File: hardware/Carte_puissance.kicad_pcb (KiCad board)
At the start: 2 copper layers, 114 x 57 mm, 41 parts, among them J1 Conn_01x02, J4 MOT LEFT, J5 MOT RIGHT, J6 Conn_01x03, Q1 IPD50P04P4-13, Q2 IPD30N03S4L-09, Q3 IPD30N03S4L-09, SW1 SW_SPDT, U1 MIC4427, U2 MCXA153VLH

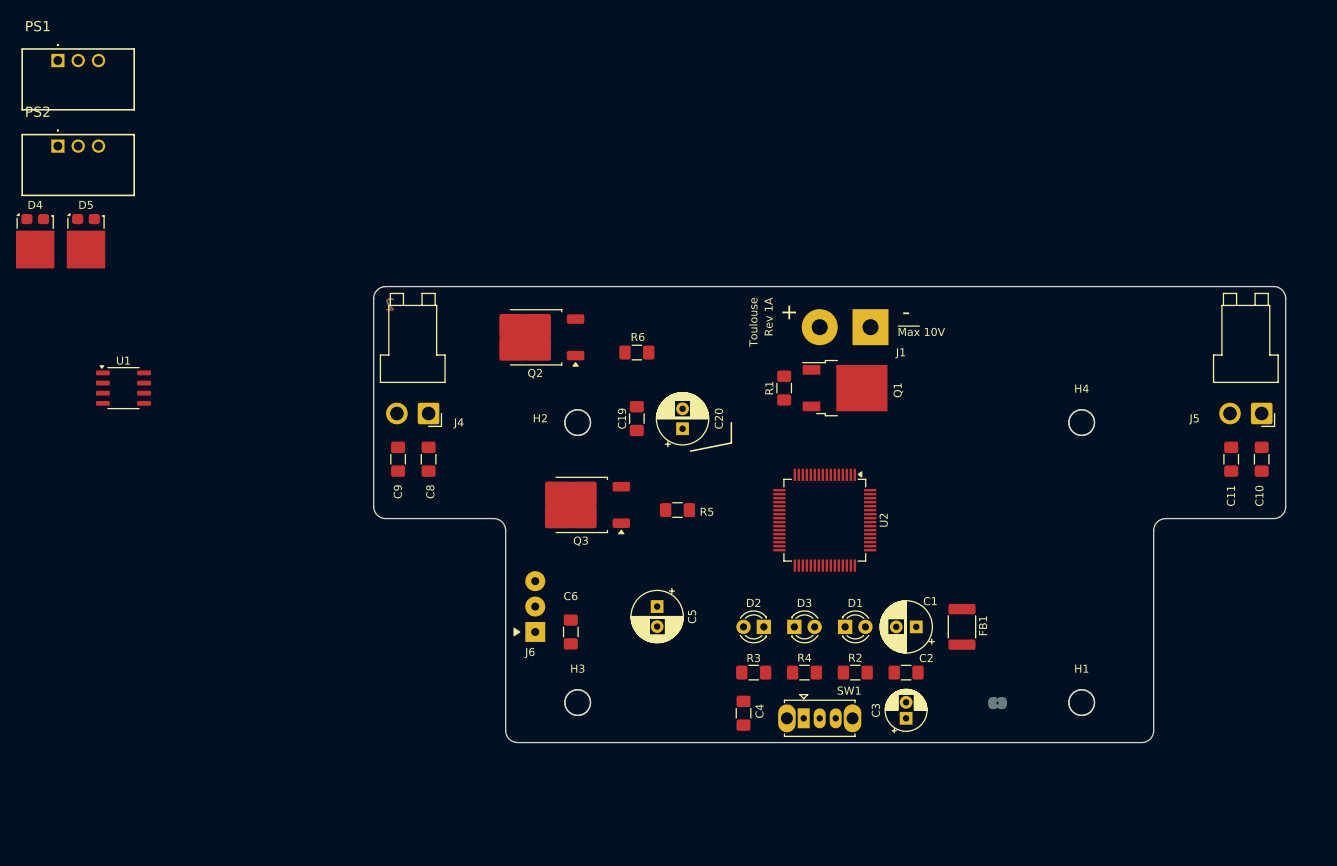
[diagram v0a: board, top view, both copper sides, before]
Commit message: Wip carte alamk pwr 2.0 prete pour tirage
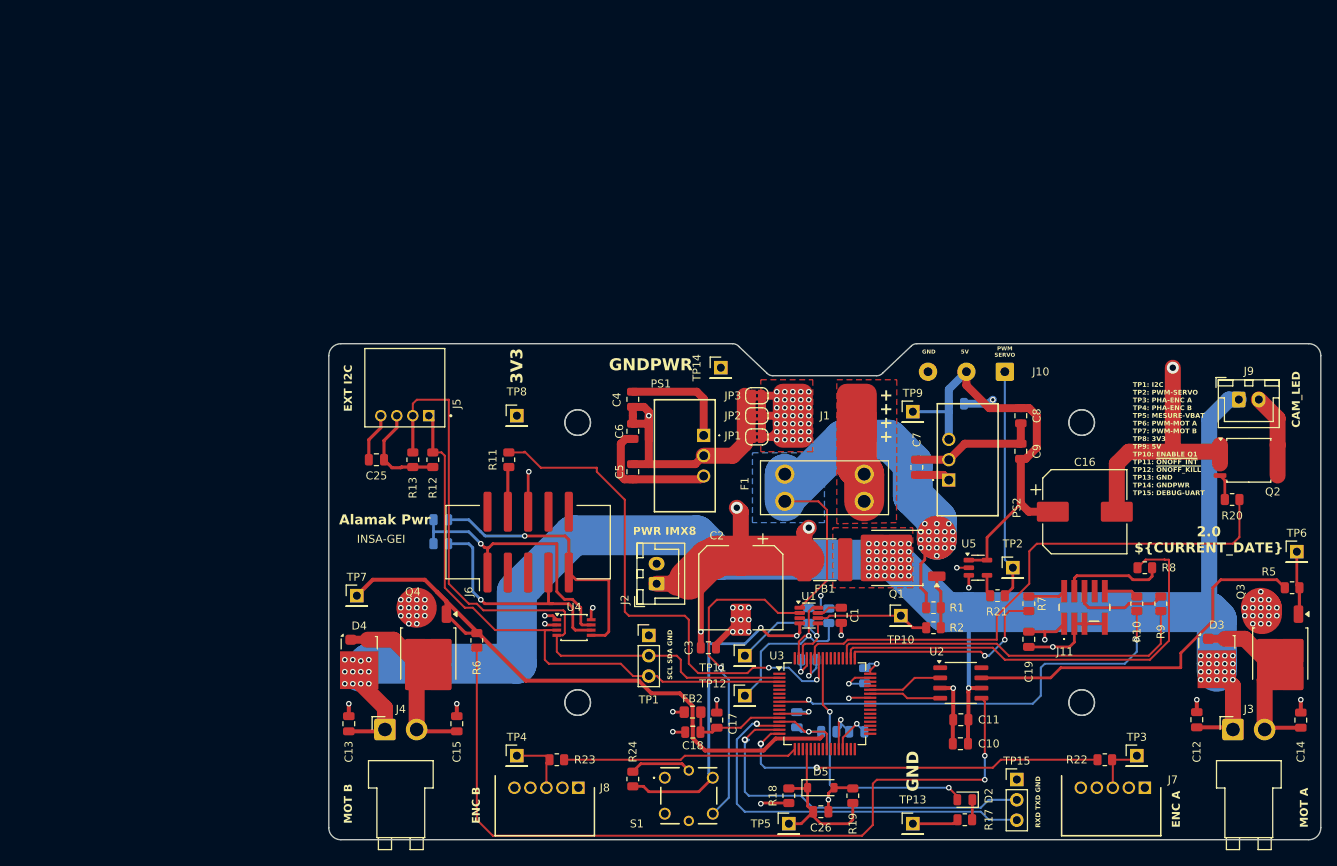
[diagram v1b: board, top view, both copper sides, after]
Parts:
- removed D1: LED, LED_THT:LED_D3.0mm
- removed SW1: SW_SPDT, Button_Switch_THT:SW_Slide_1P2T_CK_OS102011MS2Q
- added C12: 100nF, Capacitor_SMD:C_0805_2012Metric, F.Cu at (202.5, 135.1)
- added C13: 100nF, Capacitor_SMD:C_0805_2012Metric, F.Cu at (96.5, 135.6)
- added C14: 100nF, Capacitor_SMD:C_0805_2012Metric, F.Cu at (215.5, 135.1)
- added C15: 100nF, Capacitor_SMD:C_0805_2012Metric, F.Cu at (110.0, 135.6)
- added C16: 100µF, Capacitor_SMD:CP_Elec_10x10, F.Cu at (188.5, 109.1)
- added C17: 1µF, Capacitor_SMD:C_0805_2012Metric, F.Cu at (142.5, 135.1)
- added C18: 100nF, Capacitor_SMD:C_0805_2012Metric, F.Cu at (139.5, 136.6)
- added C21: 100nF, Capacitor_SMD:C_0805_2012Metric, B.Cu at (161.0, 129.6)
- added C22: 100nF, Capacitor_SMD:C_0805_2012Metric, B.Cu at (156.5, 136.6)
- added C23: 100nF, Capacitor_SMD:C_0805_2012Metric, B.Cu at (152.5, 135.1)
- added C24: 100nF, Capacitor_SMD:C_0805_2012Metric, B.Cu at (160.0, 136.6)
- added C25: 1µF, Capacitor_SMD:C_0805_2012Metric, F.Cu at (99.9, 102.6)
- added C26: 1µF, Capacitor_SMD:C_0805_2012Metric, F.Cu at (155.5, 146.6)
- added C27: 10µF, Capacitor_SMD:C_0805_2012Metric, B.Cu at (172.4, 95.6)
- added C7: 100nF, Capacitor_SMD:C_0805_2012Metric, F.Cu at (167.5, 103.5)
- added F1: Fuse - 5A, 3568:3568, F.Cu at (160.9, 104.4)
- added FB2: MH2029-401Y, Capacitor_SMD:C_0805_2012Metric_Pad1.18x1.45mm_HandSolder, F.Cu at (139.4, 134.1)
- added J10: Cable Servomoteur JST, Connector_Wire:SolderWire-0.5sqmm_1x03_P4.8mm_D0.9mm_OD2.3mm, F.Cu at (178.5, 91.6)
- added J11: FTSH-105-01-L-DV-007-K-TR, FTSH-105-01-L-DV-007:FTSH10501LDV007KTR, F.Cu at (188.4, 121.0)
- added J2: B2B-XH-2, Connector_JST:JST_XH_B2B-XH-A_1x02_P2.50mm_Vertical, F.Cu at (135.0, 118.1)
- added J3: B2PS-VH, Connector_JST:JST_VH_B2PS-VH_1x02_P3.96mm_Horizontal, F.Cu at (207.0, 136.3)
- added J7: DF3A-5P-2DS, DF3A-5P-2DS:SHDRRA5W60P0X200_1X5_1200X720X530P, F.Cu at (196.0, 143.6)
- added J8: DF3A-5P-2DS, DF3A-5P-2DS:SHDRRA5W60P0X200_1X5_1200X720X530P, F.Cu at (125.2, 143.6)
- added J9: B2B-XH-2, Connector_JST:JST_XH_B2B-XH-A_1x02_P2.50mm_Vertical, F.Cu at (207.7, 95.0)
- added JP1: SolderJumper_2_Bridged, Jumper:SolderJumper-2_P1.3mm_Bridged2Bar_RoundedPad1.0x1.5mm, F.Cu at (147.5, 99.7)
- added JP3: SolderJumper_2_Bridged, Jumper:SolderJumper-2_P1.3mm_Bridged2Bar_RoundedPad1.0x1.5mm, F.Cu at (147.5, 94.6)
- added Q4: IPD30N03S4L-09, Package_TO_SOT_SMD:TO-252-2, F.Cu at (106.4, 126.9)
- added R10: 100R, Resistor_SMD:R_0805_2012Metric, F.Cu at (195.0, 120.6)
- added R11: 100R, Resistor_SMD:R_0805_2012Metric, F.Cu at (116.5, 102.6)
- added R12: 4.7K, Resistor_SMD:R_0805_2012Metric, F.Cu at (107.0, 102.6)
- added R13: 4.7K, Resistor_SMD:R_0805_2012Metric, F.Cu at (104.5, 102.6)
- added R14: 4.7K, Resistor_SMD:R_0805_2012Metric, B.Cu at (108.0, 113.1)
- added R15: 4.7K, Resistor_SMD:R_0805_2012Metric, B.Cu at (108.0, 110.1)
- added R17: 750R, Resistor_SMD:R_0805_2012Metric, F.Cu at (173.5, 147.6)
- added R18: 18K, Resistor_SMD:R_0805_2012Metric, F.Cu at (151.5, 144.6)
- added R19: 10K, Resistor_SMD:R_0805_2012Metric, F.Cu at (159.5, 144.6)
- added R20: 10R, Resistor_SMD:R_0805_2012Metric, F.Cu at (206.9, 107.5)
- added R21: 100R, Resistor_SMD:R_0805_2012Metric, F.Cu at (177.6, 119.6)
- added R22: 100R, Resistor_SMD:R_0805_2012Metric, F.Cu at (191.0, 140.1)
- added R23: 100R, Resistor_SMD:R_0805_2012Metric, F.Cu at (122.5, 140.1)
- added R24: 330R, Resistor_SMD:R_0805_2012Metric, F.Cu at (132.0, 142.5)
- added R7: 100R, Resistor_SMD:R_0805_2012Metric, F.Cu at (181.5, 120.6)
- added R8: 100R, Resistor_SMD:R_0805_2012Metric, F.Cu at (196.0, 116.1)
- added R9: 100R, Resistor_SMD:R_0805_2012Metric, F.Cu at (198.0, 120.6)
- added S1: TL1265BQSCLR, TL1265BQSCLR:TL1265BQSCLR, F.Cu at (136.0, 142.3)
- added TP1: Conn_01x03_Pin, Connector_PinHeader_2.54mm:PinHeader_1x03_P2.54mm_Vertical, F.Cu at (134.0, 124.5)
- added TP10: TestPoint, Connector_PinHeader_2.54mm:PinHeader_1x01_P2.54mm_Vertical, F.Cu at (165.5, 122.1)
- added TP11: TestPoint, Connector_PinHeader_2.54mm:PinHeader_1x01_P2.54mm_Vertical, F.Cu at (146.0, 127.1)
- added TP12: TestPoint, Connector_PinHeader_2.54mm:PinHeader_1x01_P2.54mm_Vertical, F.Cu at (146.0, 132.1)
- added TP13: TestPoint, Connector_PinHeader_2.54mm:PinHeader_1x01_P2.54mm_Vertical, F.Cu at (167.0, 148.1)
- added TP14: TestPoint, Connector_PinHeader_2.54mm:PinHeader_1x01_P2.54mm_Vertical, F.Cu at (143.0, 91.1)
- added TP15: Conn_01x03_Pin, Connector_PinHeader_2.54mm:PinHeader_1x03_P2.54mm_Vertical, F.Cu at (180.0, 142.5)
- added TP2: TestPoint, Connector_PinHeader_2.54mm:PinHeader_1x01_P2.54mm_Vertical, F.Cu at (179.5, 116.1)
- added TP3: TestPoint, Connector_PinHeader_2.54mm:PinHeader_1x01_P2.54mm_Vertical, F.Cu at (195.0, 139.6)
- added TP4: TestPoint, Connector_PinHeader_2.54mm:PinHeader_1x01_P2.54mm_Vertical, F.Cu at (117.5, 139.6)
- added TP5: TestPoint, Connector_PinHeader_2.54mm:PinHeader_1x01_P2.54mm_Vertical, F.Cu at (151.5, 148.1)
- added TP6: TestPoint, Connector_PinHeader_2.54mm:PinHeader_1x01_P2.54mm_Vertical, F.Cu at (215.0, 114.1)
- added TP7: TestPoint, Connector_PinHeader_2.54mm:PinHeader_1x01_P2.54mm_Vertical, F.Cu at (97.5, 119.6)
- added TP8: TestPoint, Connector_PinHeader_2.54mm:PinHeader_1x01_P2.54mm_Vertical, F.Cu at (117.5, 97.1)
- added TP9: TestPoint, Connector_PinHeader_2.54mm:PinHeader_1x01_P2.54mm_Vertical, F.Cu at (167.0, 96.6)
- added U3: MCXA153VLH, Package_QFP:LQFP-64_10x10mm_P0.5mm, F.Cu at (156.0, 133.1)
- added U4: PCA9306DP, Package_SO:TSSOP-8_3x3mm_P0.65mm, F.Cu at (124.6, 123.5)
- added U5: 74AHC1G126, Package_TO_SOT_SMD:SOT-23-5, F.Cu at (175.1, 116.1)
- C1: value 100µF -> 1µF; footprint Capacitor_THT:CP_Radial_D6.3mm_P2.50mm -> Capacitor_SMD:C_0805_2012Metric
- C10, C4, C8: footprint Capacitor_SMD:C_1206_3216Metric_Pad1.42x1.75mm_HandSolder -> Capacitor_SMD:C_0805_2012Metric
- C11, C6, C9: value 100nF -> 10µF; footprint Capacitor_SMD:C_1206_3216Metric_Pad1.42x1.75mm_HandSolder -> Capacitor_SMD:C_0805_2012Metric
- C19: value 100nF -> 470nF; footprint Capacitor_SMD:C_1206_3216Metric_Pad1.42x1.75mm_HandSolder -> Capacitor_SMD:C_0805_2012Metric
- C2: value 100nF -> 100µF; footprint Capacitor_SMD:C_1206_3216Metric_Pad1.42x1.75mm_HandSolder -> Capacitor_SMD:CP_Elec_10x10
- C20: value 470µF -> 100nF; footprint Capacitor_THT:CP_Radial_D6.3mm_P2.50mm -> Capacitor_SMD:C_0805_2012Metric; moved to B.Cu
- C3: footprint Capacitor_THT:CP_Radial_D5.0mm_P2.00mm -> Capacitor_SMD:C_0805_2012Metric
- C5: value 100µF -> 100nF; footprint Capacitor_THT:CP_Radial_D6.3mm_P2.50mm -> Capacitor_SMD:C_0805_2012Metric
- D2: value LED -> LED Rouge; footprint LED_THT:LED_D3.0mm -> LED_SMD:LED_0805_2012Metric
- D3: value LED -> STPS1230SF; footprint LED_THT:LED_D3.0mm -> Package_TO_SOT_SMD:TO-277A
- D5: value STPS1230SF -> MMSZ3V3T1G; footprint Package_TO_SOT_SMD:TO-277A -> Diode_SMD:D_SOD-123
- FB1: value Ferrite_Bead -> 7427928801; footprint Capacitor_SMD:C_1812_4532Metric_Pad1.30x3.40mm_HandSolder -> Capacitor_SMD:C_2220_5750Metric
- J1: value Conn_01x02 -> Cable XT60; footprint Connector_Wire:SolderWirePad_1x02_P7.62mm_Drill2mm -> Battery_Pads:Battery_Pads
- J4: value MOT LEFT -> B2PS-VH
- J5: value MOT RIGHT -> SeedStudio 110990037; footprint Connector_JST:JST_VH_B2PS-VH_1x02_P3.96mm_Horizontal -> Seeed Studio 110990037:SEEED_110990037
- J6: value Conn_01x03 -> 72454-010VLF; footprint Connector_Wire:SolderWirePad_1x03_P3.175mm_Drill1mm -> Connector_IDC:IDC-Header_2x05_P2.54mm_Vertical_SMD
- JP2: moved to F.Cu
- Q1: value IPD50P04P4-13 -> IPD50P04P413ATMA2
- Q2: value IPD30N03S4L-09 -> TPH2R506PL,L1Q; footprint Package_TO_SOT_SMD:TO-252-2 -> Package_SO:SOP-8_5.28x5.23mm_P1.27mm
- R1: value 10K -> 100K; footprint Resistor_SMD:R_1206_3216Metric_Pad1.42x1.75mm_HandSolder -> Resistor_SMD:R_0805_2012Metric
- R2: value 470R -> 100K; footprint Resistor_SMD:R_1206_3216Metric_Pad1.42x1.75mm_HandSolder -> Resistor_SMD:R_0805_2012Metric
- R3: value 220R -> 10K; footprint Resistor_SMD:R_1206_3216Metric_Pad1.42x1.75mm_HandSolder -> Resistor_SMD:R_0805_2012Metric; moved to B.Cu
- R4: value 100R -> 10K; footprint Resistor_SMD:R_1206_3216Metric_Pad1.42x1.75mm_HandSolder -> Resistor_SMD:R_0805_2012Metric; moved to B.Cu
- R5, R6: value 10K -> 10R; footprint Resistor_SMD:R_1206_3216Metric_Pad1.42x1.75mm_HandSolder -> Resistor_SMD:R_0805_2012Metric
- U1: value MIC4427 -> LTC2954CTS8-2#TRMPBF; footprint Package_SO:SO-8_3.9x4.9mm_P1.27mm -> Package_TO_SOT_SMD:SOT-23-8
- U2: value MCXA153VLH -> MIC4427; footprint Package_QFP:LQFP-64_10x10mm_P0.5mm -> Package_SO:SO-8_3.9x4.9mm_P1.27mm
- moved PS2 118.9 mm to (171.5, 105.1), turned to 90 degrees
- moved D5 114.5 mm to (155.5, 143.6)
- moved J5 107.2 mm to (103.5, 93.6)
- moved PS1 93.3 mm to (140.8, 99.5), turned to -90 degrees
- moved Q2 90.5 mm to (209.0, 102.6), turned to 0 degrees
- moved U1 90.3 mm to (154.0, 122.0)
- moved Q3 89.4 mm to (212.9, 126.9), turned to -90 degrees
- moved C9 77.8 mm to (180.5, 101.5), turned to 90 degrees
- moved R5 77.4 mm to (214.4, 118.6)
- moved C8 74.2 mm to (180.5, 97.1), turned to -90 degrees
- moved D4 66.4 mm to (97.8, 127.8)
- moved C19 56.2 mm to (181.5, 125.0), turned to -90 degrees
- moved D3 53.0 mm to (205.0, 127.7)
- moved C10 51.8 mm to (172.9, 138.1), turned to 180 degrees
- moved C11 46.9 mm to (173.0, 135.1), turned to 180 degrees
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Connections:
- C1 pad 1: VCC -> Net-(U1-PDT)
- C1 pad 2: GND -> GNDPWR
- C10 pad 1: GNDPWR -> +BATT
- C10 pad 2: +BATT -> GNDPWR
- C11 pad 1: Net-(D5-A) -> +BATT
- C19 pad 1: +BATT -> +3.3V
- C19 pad 2: GNDPWR -> GND
- C20 pad 1: +BATT -> +3.3V
- C20 pad 2: GNDPWR -> GND
- C3 pad 1: +3V3 -> VCC
- C5 pad 1: +5V -> +3.3V
- C5 pad 2: GNDA -> GND
- C6 pad 1: GNDA -> +3.3V
- C6 pad 2: +5V -> GND
- C8 pad 1: GNDPWR -> +5V
- C8 pad 2: +BATT -> GNDPWR
- C9 pad 1: Net-(D4-A) -> +5V
- D2 pad 2: +5V -> /CPU/ALERT_LED
- D3 pad 1: Net-(D3-K) -> Net-(J3-Pin_2)
- D3 pad 2: +3.3V -> Net-(J3-Pin_2)
- D4 pad 1: +BATT -> Net-(J4-Pin_2)
- D4 pad 2: Net-(D4-A) -> Net-(J4-Pin_2)
- D4 pad 3: (no net) -> +BATT
- D5 pad 1: +BATT -> /CPU/MESURE_ADC
- D5 pad 2: Net-(D5-A) -> GND
- FB1 pad 1: VCC -> +BATT
- FB1 pad 2: +BATT -> VCC
- J4 pad 2: Net-(D4-A) -> Net-(J4-Pin_2)
- J5 pad 1: +BATT -> /CPU/I2C_SCL
- J5 pad 2: Net-(D5-A) -> /CPU/I2C_SDA
- J6 pad 1: /SERVO_PWM -> /IO/3V3_IMX8MP
- J6 pad 2: +5V -> unconnected-(J6-Pin_2-Pad2)
- J6 pad 3: GNDA -> unconnected-(J6-Pin_3-Pad3)
- PS2 pad 2: GND -> GNDPWR
- Q1 pad 3: Net-(J1-Pin_2) -> Net-(Q1-S)
- Q2 pad 1: Net-(Q2-G) -> GNDPWR
- Q2 pad 2: Net-(D4-A) -> GNDPWR
- Q3 pad 2: Net-(D5-A) -> Net-(J3-Pin_2)
- R1 pad 1: Net-(J1-Pin_2) -> Net-(Q1-S)
- R2 pad 1: Net-(D1-K) -> Net-(U1-EN/~{EN})
- R2 pad 2: GND -> Net-(Q1-G)
- R3 pad 1: Net-(D2-K) -> +3.3V
- R3 pad 2: GND -> /CPU/~{ONOFF_INT}
- R4 pad 1: Net-(D3-K) -> +3.3V
- R4 pad 2: GND -> /CPU/~{ONOFF_KILL}
- R5 pad 1: /DISABLE_MOT_L -> Net-(Q3-G)
- R5 pad 2: Net-(Q3-Pad3) -> Net-(U2-OUT_A)
- R6 pad 1: /DISABLE_MOT_L -> Net-(U2-OUT_B)
- U1 pad 1: unconnected-(U1-NC-Pad1) -> Net-(Q1-S)
- U1 pad 2: unconnected-(U1-IN_A-Pad2) -> Net-(S1-NO_4)
- U1 pad 3: GNDPWR -> unconnected-(U1-ONT-Pad3)
- U1 pad 4: unconnected-(U1-IN_B-Pad4) -> GNDPWR
- U1 pad 5: Net-(U1-OUT_B) -> /CPU/~{ONOFF_INT}
- U1 pad 6: +BATT -> Net-(U1-EN/~{EN})
- U1 pad 7: Net-(U1-OUT_A) -> Net-(U1-PDT)
- U1 pad 8: unconnected-(U1-NC-Pad8) -> /CPU/~{ONOFF_KILL}
- U2 pad 2: unconnected-(U2-P1_8/WUU0_IN10/LPUART1_RXD/LPI2C0_SDA/CT_INP8/CT0_MAT2/I3C0_SDA-Pad2) -> /CPU/MOTOR_A_PWM
- U2 pad 3: unconnected-(U2-P1_9/LPUART1_TXD/LPI2C0_SCL/CT_INP9/CT0_MAT3/I3C0_SCL-Pad3) -> GNDPWR
- U2 pad 4: unconnected-(U2-P1_10/LPUART1_RTS_B/LPI2C0_SDAS/CT2_MAT0/ADC0_A8-Pad4) -> /CPU/MOTOR_B_PWM
- U2 pad 5: unconnected-(U2-P1_11/WUU0_IN11/TRIG_OUT2/LPUART1_CTS_B/LPI2C0_SCLS/CT2_MAT1/I3C0_PUR/ADC0_A9-Pad5) -> Net-(U2-OUT_B)
- U2 pad 6: unconnected-(U2-P1_12/WUU0_IN12/LPUART2_RXD/CT2_MAT2/ADC0_A10-Pad6) -> +BATT
- U2 pad 7: unconnected-(U2-P1_13/TRIG_IN3/LPUART2_TXD/CT2_MAT3/ADC0_A11-Pad7) -> Net-(U2-OUT_A)
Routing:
- net GNDPWR: track 0.00 -> 408.8 mm, vias 0 -> 76
- net +BATT: track 0.00 -> 202.5 mm, vias 0 -> 63
- net VCC: track 0.00 -> 122.1 mm, vias 0 -> 4
- net GND: track 0.00 -> 108.7 mm, vias 0 -> 21
- net Net-(U2-OUT_B): track 0.00 -> 102.1 mm, vias 0 -> 2
- net /CPU/I2C_SDA: track 0.00 -> 85.6 mm
- net Net-(Q4-G): track 0.00 -> 79.0 mm
- net /CPU/I2C_SCL: track 0.00 -> 74.0 mm
- net /CPU/CMD_CAMERA_LED: track 0.00 -> 69.0 mm
- net +3.3V: track 0.00 -> 68.7 mm, vias 0 -> 9
- net /CPU/ONOFF_IMX8MP: track 0.00 -> 65.5 mm, vias 0 -> 2
- net Net-(Q1-S): track 0.00 -> 65.5 mm, vias 0 -> 19
- net /CPU/SWCLK: track 0.00 -> 57.0 mm
- net /CPU/nRESET: track 0.00 -> 54.8 mm, vias 0 -> 2
- net +5V: track 0.00 -> 53.6 mm
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- added copper zone on In1.Cu, net +3.3V
- added copper zone on F.Cu, net +BATT
- added copper zone on In2.Cu, net GND
- added copper zone on F.Cu, net GNDPWR
- added copper zone on In2.Cu, net GNDPWR
- added copper zone on F.Cu, net Net-(J1-Pin_2)
- added copper zone on B.Cu, net Net-(Q1-S)
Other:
- board size 114 x 57 mm -> 124 x 62 mm
- copper layers 2 -> 4
- rule pad_to_mask_clearance: 0.051 -> 0
- board text added: "${COMPANY}"
- board text added: "${REVISION} ${CURRENT_DATE}"
- board text added: "${TITLE}"
- board text added: "++++"
- board text added: "3V3"
- board text added: "5V"
- board text added: "Arriere"
- board text added: "Avant"
- board text added: "CAM_LED"
- board text added: "ENC A"
- board text added: "ENC B"
- board text added: "EXT I2C"
- board text added: "GND"
- board text added: "GNDPWR"
- board text added: "IDX 3.3V PHA PHB GND"
- board text added: "MOT A"
- board text added: "MOT B"
- board text added: "PWM SERVO"
- board text added: "PWR IMX8"
- board text added: "RXD TXD GND"
- board text added: "SCL SDA 3.3V GND"
- board text added: "SCL SDA GND"
- board text added: "TP1: I2C TP2: PWM-SERVO TP3: PHA-ENC A TP4: PHA-ENC B TP5: MESURE-VBAT TP6: PWM-MOT A TP7: PWM-MOT B TP8: 3V3 TP9: 5V TP10: ENABLE Q1 TP11: ~{ONOFF_INT} TP12: ~{ONOFF_KILL} TP13: GND TP14: GNDPWR TP15: DEBUG-UART"
- board text removed: "+"
- board text removed: "-"
- board text removed: "1"
- board text removed: "2"
- board text removed: "Rev 1A"
- board text removed: "Toulouse"
- board text removed: "~{Max} 10V"

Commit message: Wip correction sur le connecteur debug et realisation d'un soft de test pour verifier le mapping des fonctions sur les pins
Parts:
- R10, R7, R8: value 100R -> 100K
- R9: value 100R -> 2.2K
- moved R10 2.69 mm to (196.0, 123.1), turned to 0 degrees
- moved R9 2.24 mm to (196.0, 119.6), turned to 180 degrees
- moved R8 0.50 mm to (196.0, 116.6)
- turned R7 to 90 degrees
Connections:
- J11 pad 10: Net-(J11-Pad10) -> /CPU/nRESET
- J11 pad 2: Net-(J11-Pad2) -> /CPU/SWDIO
- J11 pad 4: Net-(J11-Pad4) -> /CPU/SWCLK
- J11 pad 6: Net-(J11-Pad6) -> /CPU/SWO
- J11 pad 9: GND -> Net-(J11-Pad9)
- R10 pad 1: Net-(J11-Pad10) -> /CPU/nRESET
- R10 pad 2: /CPU/nRESET -> +3.3V
- R7 pad 1: Net-(J11-Pad2) -> /CPU/SWDIO
- R7 pad 2: /CPU/SWDIO -> +3.3V
- R8 pad 1: Net-(J11-Pad4) -> GND
- R9 pad 1: Net-(J11-Pad6) -> GND
- R9 pad 2: /CPU/SWO -> Net-(J11-Pad9)
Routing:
- net Net-(Q4-G): track 79.0 -> 19.5 mm
- net Net-(J11-Pad4): track 12.9 -> 0.00 mm
- net Net-(J11-Pad6): track 11.9 -> 0.00 mm
- net /CPU/SWCLK: track 57.0 -> 46.4 mm, vias 0 -> 2
- net /CPU/nRESET: track 54.8 -> 64.5 mm
- net Net-(J11-Pad9): track 0.00 -> 7.00 mm
- net /CPU/SWDIO: track 26.9 -> 32.9 mm
- net /CPU/SWO: track 46.3 -> 41.3 mm
- net Net-(J11-Pad2): track 4.69 -> 0.00 mm
- net Net-(J11-Pad10): track 4.27 -> 0.00 mm
- net +3.3V: track 68.7 -> 73.0 mm, vias 9 -> 11
- net GND: track 108.7 -> 109.2 mm, vias 21 -> 22
